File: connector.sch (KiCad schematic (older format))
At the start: 6 parts, among them J1 Bus_M.2_Socket_B

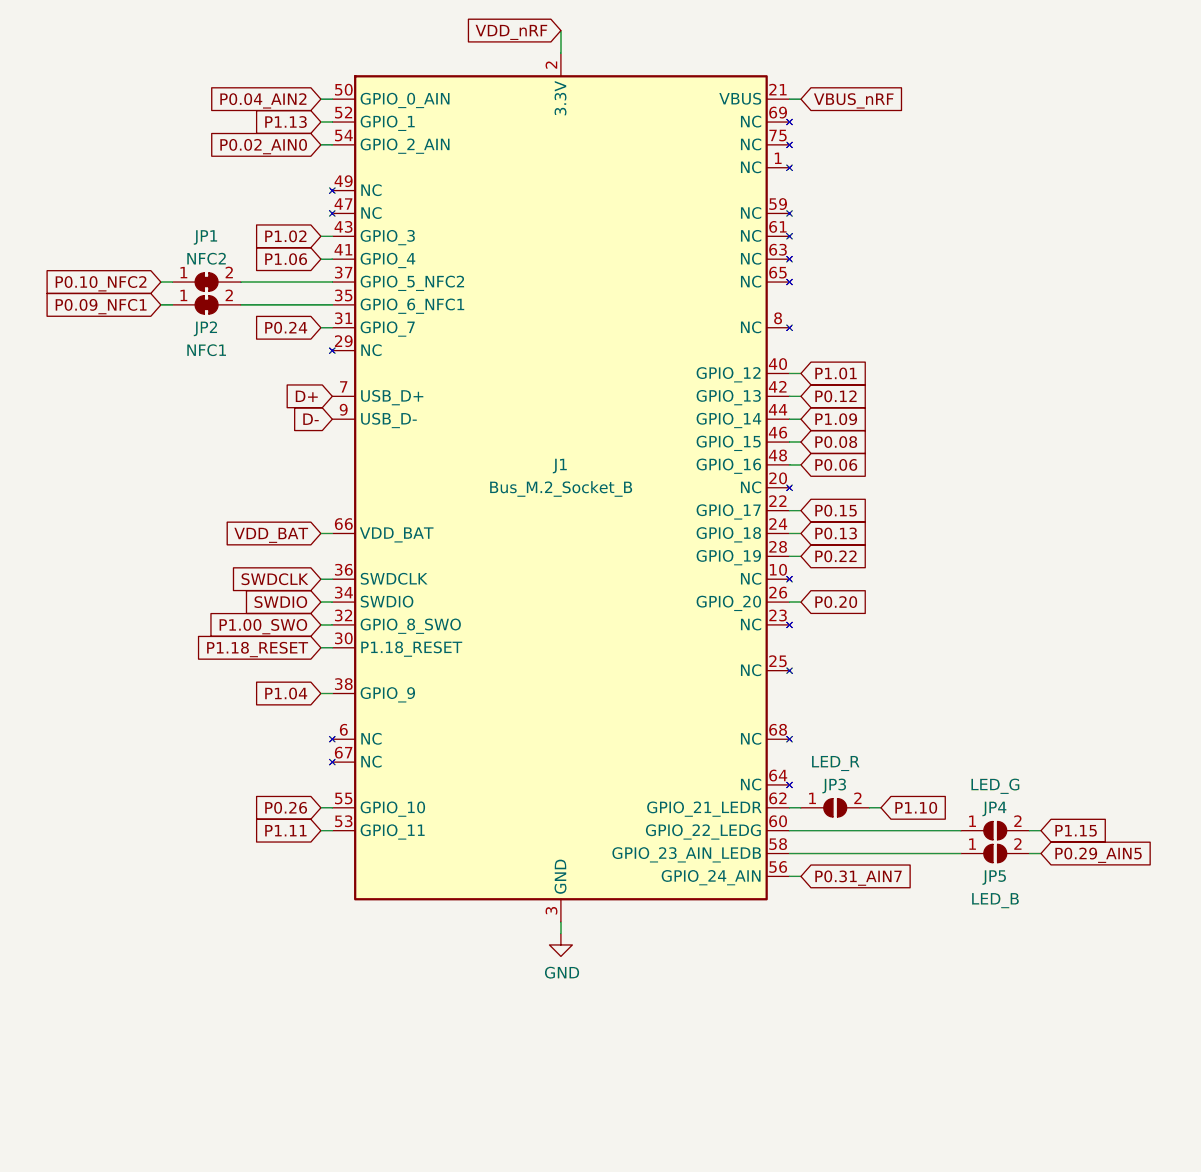
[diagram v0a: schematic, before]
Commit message: update 3D/docs/fiducials
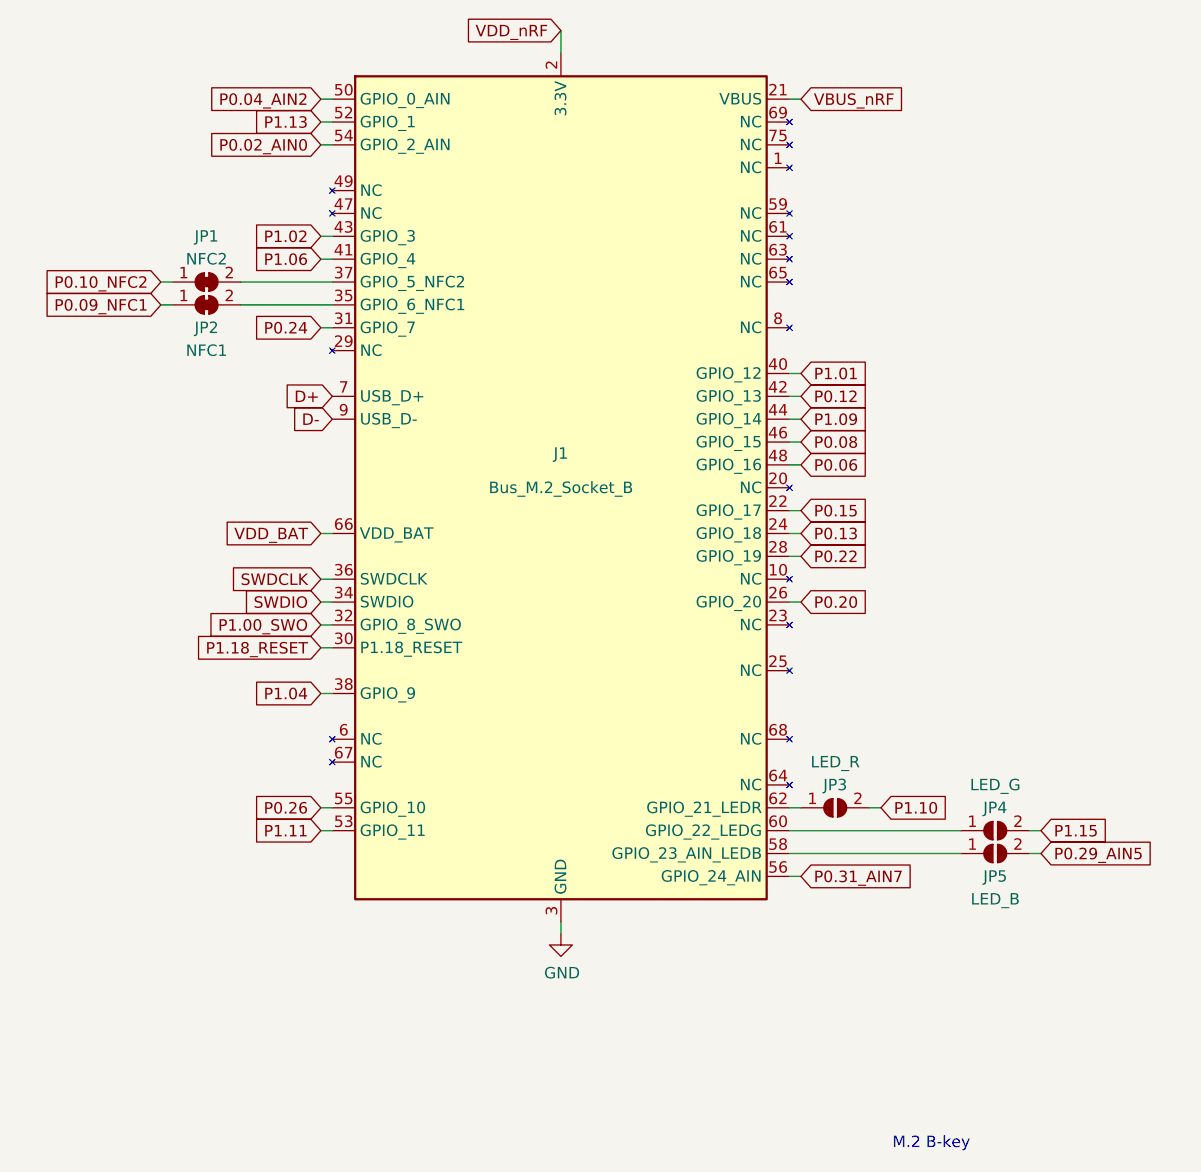
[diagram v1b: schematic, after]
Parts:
- J1, JP1, JP2, JP3, JP4, JP5: DNP (none) -> DNP
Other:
- note added: "M.2 B-key"
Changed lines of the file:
@@
 Date "2020-12-02"
 Rev "0.1"
-Comp "crohloff"
+Comp "crohloff Engineering"
 Comment1 ""
 Comment2 ""
@@
 F 1 "NFC1" H 4000 2750 50  0000 C CNN
 F 2 "custom_footprints:solder_bridge_closed" H 4000 2950 50  0001 C CNN
-F 3 "~" H 4000 2950 50  0001 C CNN
+F 3 "" H 4000 2950 50  0001 C CNN
+F 4 "DNP" H 4000 2950 50  0001 C CNN "DNP"
 	1    4000 2950
 	1    0    0    -1
@@
 F 1 "NFC2" H 4000 2950 50  0000 C CNN
 F 2 "custom_footprints:solder_bridge_closed" H 4000 2850 50  0001 C CNN
-F 3 "~" H 4000 2850 50  0001 C CNN
+F 3 "" H 4000 2850 50  0001 C CNN
+F 4 "DNP" H 4000 2850 50  0001 C CNN "DNP"
 	1    4000 2850
 	1    0    0    -1
@@
 F 1 "LED_R" H 6750 5350 50  0000 C CNN
 F 2 "custom_footprints:solder_bridge_open" H 6750 5150 50  0001 C CNN
-F 3 "~" H 6750 5150 50  0001 C CNN
+F 3 "" H 6750 5150 50  0001 C CNN
+F 4 "DNP" H 6750 5150 50  0001 C CNN "DNP"
 	1    6750 5150
 	1    0    0    -1
@@
 F 1 "LED_G" H 7450 5450 50  0000 C CNN
 F 2 "custom_footprints:solder_bridge_open" H 7450 5250 50  0001 C CNN
-F 3 "~" H 7450 5250 50  0001 C CNN
+F 3 "" H 7450 5250 50  0001 C CNN
+F 4 "DNP" H 7450 5250 50  0001 C CNN "DNP"
 	1    7450 5250
 	1    0    0    -1
@@
 F 1 "LED_B" H 7450 5150 50  0000 C CNN
 F 2 "custom_footprints:solder_bridge_open" H 7450 5350 50  0001 C CNN
-F 3 "~" H 7450 5350 50  0001 C CNN
+F 3 "" H 7450 5350 50  0001 C CNN
+F 4 "DNP" H 7450 5350 50  0001 C CNN "DNP"
 	1    7450 5350
 	1    0    0    -1
@@
 Wire Wire Line
 	6550 5350 7300 5350
-$Comp
-L bus_m.2_socket_b:Bus_M.2_Socket_B J?
-U 1 1 604A8D05
+Wire Wire Line
+	6550 5150 6600 5150
+Wire Wire Line
+	6550 5450 6600 5450
+Wire Wire Line
+	4500 3050 4550 3050
+$Comp
+L bus_m.2_socket_b:Bus_M.2_Socket_B J1
+U 1 1 5FD7D178
 P 5550 3750
-AR Path="/604A8D05" Ref="J?"  Part="1"
-AR Path="/60498718/604A8D05" Ref="J1"  Part="1"
-F 0 "J1" H 5550 3850 50  0000 C CNN
+F 0 "J1" H 5550 3900 50  0000 C CNN
 F 1 "Bus_M.2_Socket_B" H 5550 3750 50  0000 C CNN
 F 2 "custom_footprints:NGFF_B" H 5550 4800 50  0001 C CNN
-F 3 "http://read.pudn.com/downloads794/doc/project/3133918/PCIe_M.2_Electromechanical_Spec_Rev1.0_Final_11012013_RS_Clean.pdf#page=154" H 5550 4800 50  0001 C CNN
+F 3 "" H 5550 4800 50  0001 C CNN
+F 4 "DNP" H 5550 3750 50  0001 C CNN "DNP"
 	1    5550 3750
 	1    0    0    -1
 $EndComp
-Wire Wire Line
-	6550 5150 6600 5150
-Wire Wire Line
-	6550 5450 6600 5450
-Wire Wire Line
-	4500 3050 4550 3050
+Text Notes 7000 6650 0    50   ~ 0
+M.2 B-key
 $EndSCHEMATC
